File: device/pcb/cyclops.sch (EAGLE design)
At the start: 184 parts, among them Q1 NDS351AN, Q2 NDS351AN, Q4 IRF510, U1 MCP4921, U10 ADG1201, U11 THS4281, U12 MAX4564, U13 ZXTD, U14 ZXTD, U15 OPA1664, U16 LTM8020, U2 LT1931, U3 LT1764A, U4 BD00FC0WEFJ, U5 TPS72325, U6 LT1711, U69 FDN352AP, U7 TLV3701, U8 ADR03, U9 LT1880

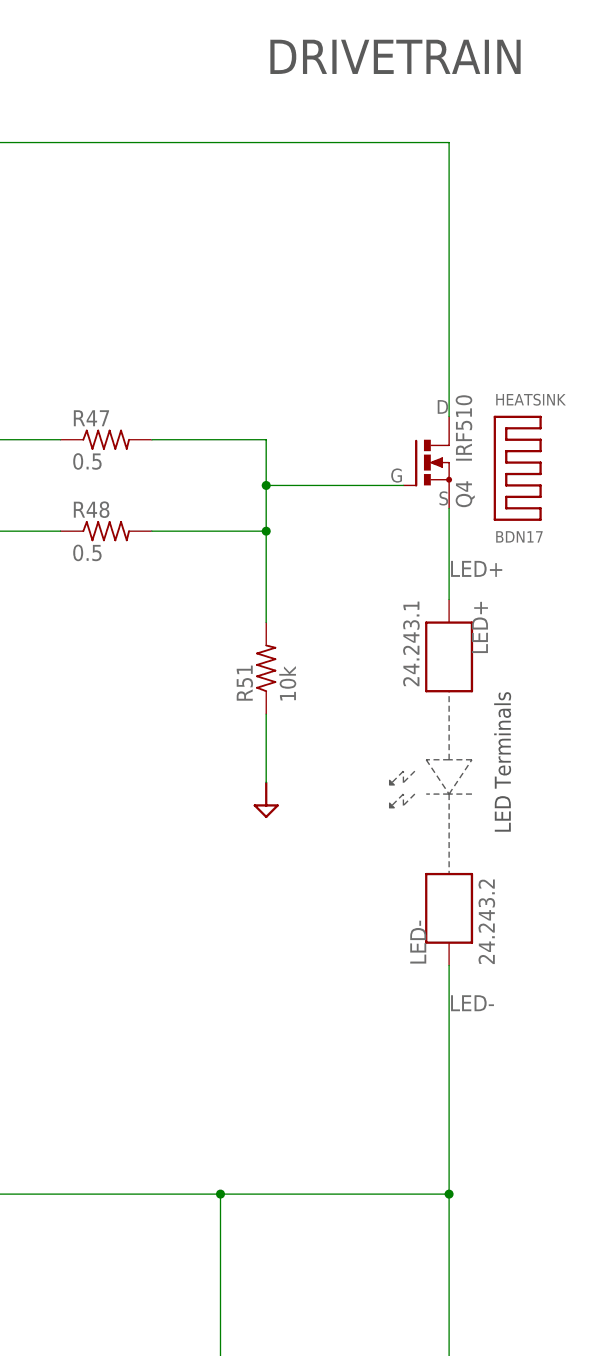
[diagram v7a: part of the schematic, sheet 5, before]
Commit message: Moved the LED to drain side of FET
- This prevents Vgs from dropping in nonlinear fashion as LED turns on.
  Not sure why LED was on low side to begin with.
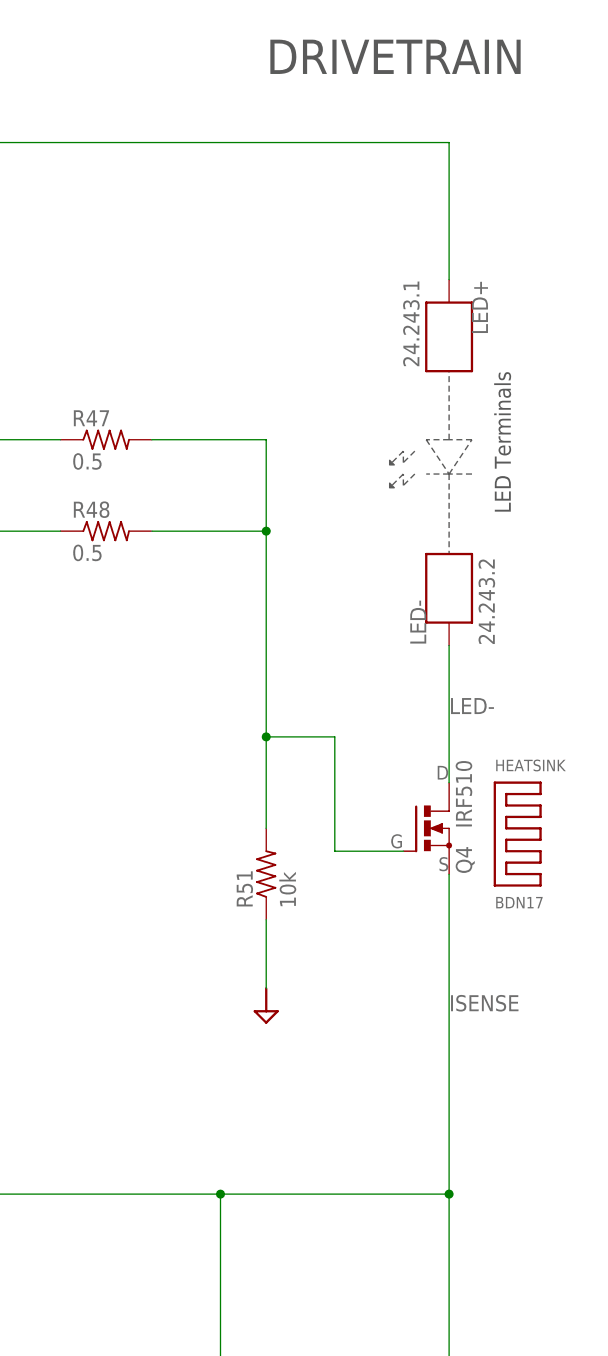
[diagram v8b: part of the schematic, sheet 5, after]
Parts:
- removed U69: FDN352AP, jonnew:P-MOSFET_SOT23-GSD
- added Q3: NDS351AN, jonnew:N-MOSFET_SOT23-GSD
- renumbered VREF<>TTL1 to VCTL<>CONT
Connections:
- removed net LED+: EXPANSION_A.1, EXPANSION_A.2, LED+.1, Q4.S
- removed net N$16: R30.2, U69.D
- new net ISENSE: Q4.S, RSENSE.2, U12.NC, U15A.+IN, U15C.+IN
- net +13.3V: now also EXPANSION_A.1, EXPANSION_A.2, LED+.1; no longer Q4.D
- net +6V: now also R30.2; no longer R29.1, U69.S
- net GND: now also Q3.S, R29.1
- net LED-: now also Q4.D; no longer RSENSE.2, U12.NC, U15A.+IN, U15C.+IN
- net N$39: now also Q3.G; no longer U69.G
- net N$41: now also Q3.D
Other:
- moved on the sheet: HEATSINK, LED+, LED-, OC2, Q4, R29, R30, R51
